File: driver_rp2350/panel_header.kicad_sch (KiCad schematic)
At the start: 4 parts, among them J6 Conn_01x05, J7 Conn_01x05, J8 Conn_01x05, J9 Conn_01x05

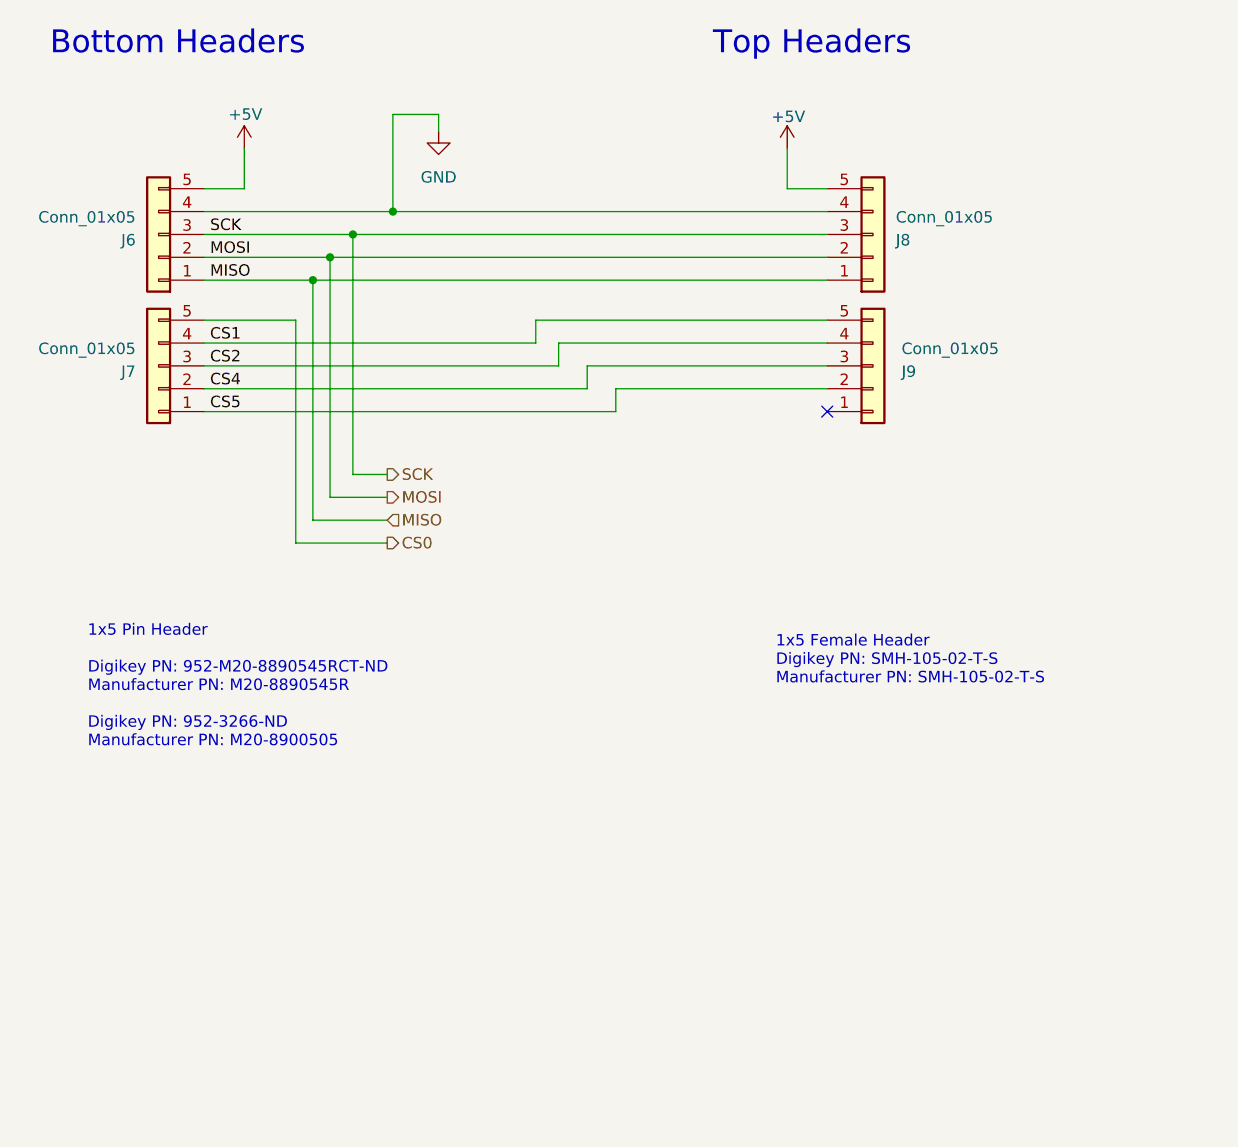
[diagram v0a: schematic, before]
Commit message: Finished first version of schematic for rp2350 G6 panel.
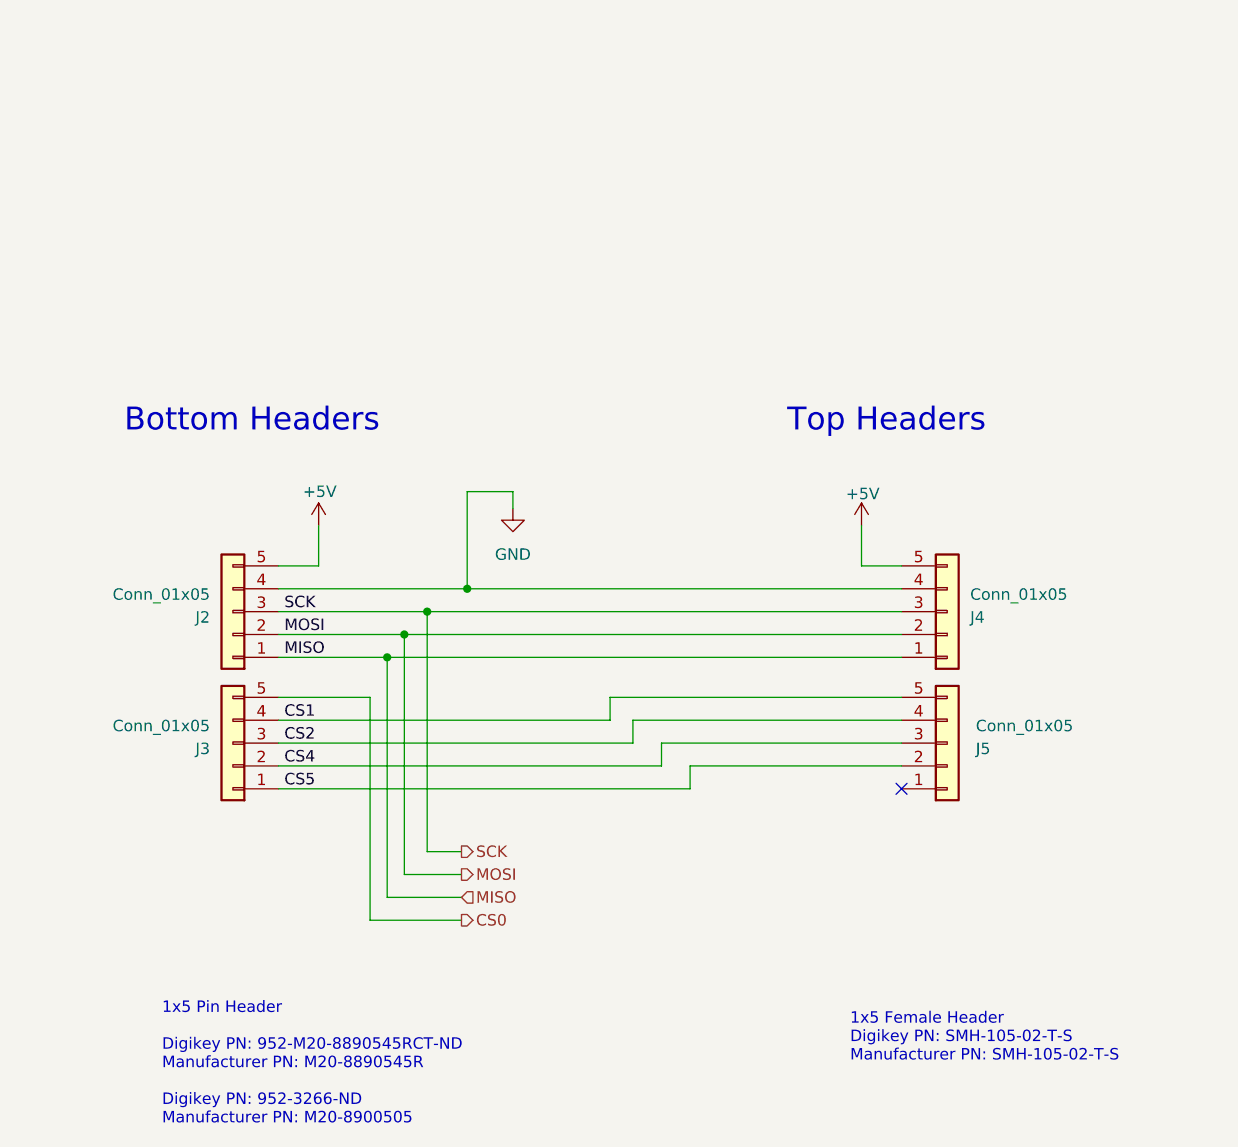
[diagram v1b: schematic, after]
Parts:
- renumbered J6 to J2, J7 to J3, J8 to J4, J9 to J5
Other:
- moved on the sheet: J2, J3, J4, J5
